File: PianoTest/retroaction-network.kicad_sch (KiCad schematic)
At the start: 64 parts, among them U201 MCP23S17-E/ML, U202 TMUX1112RSVR, U203 TMUX1112RSVR, U204 BGSA142GN12, U205 BGSA142GN12

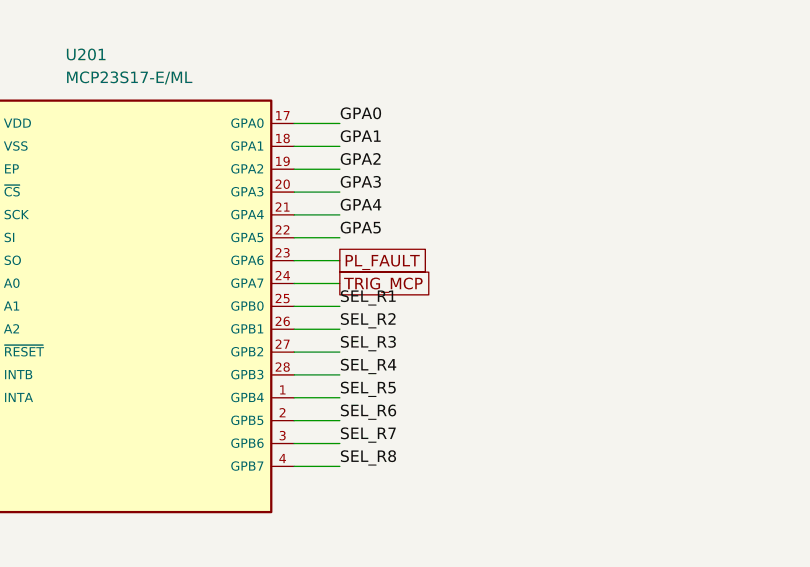
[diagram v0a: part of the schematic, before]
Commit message: PianoTest: discriminatore, latch e rilevatore di picco
Comparatore TLV3501 su SHAPER_OUT con soglia dal canale B del DAC61402
(partitore 22k/10k, BAT54S), latch 74LVC1G74 su GPA7 dell'MCP (ALERT#),
uscita HIT su TP e SMA. Rilevatore di picco OPA2365 + BAS416 + hold 1 nF
C0G prima dell'ADS8326, con reset da accesso SPI all'indirizzo 3 e
ponticello 0R per scavalcarlo. Trigger del LED dallo strobe dell'indirizzo 4.
Articolo: sezione 3.1 (formatore e acquisizione) aggiornata e ricompilata.
ERC 0.

Co-Authored-By: Claude Opus 5.5 (1M context) <noreply@anthropic.com>
Claude-Session: https://claude.ai/code/session_01J3krgWFTUEjwvCnwUp9cQn
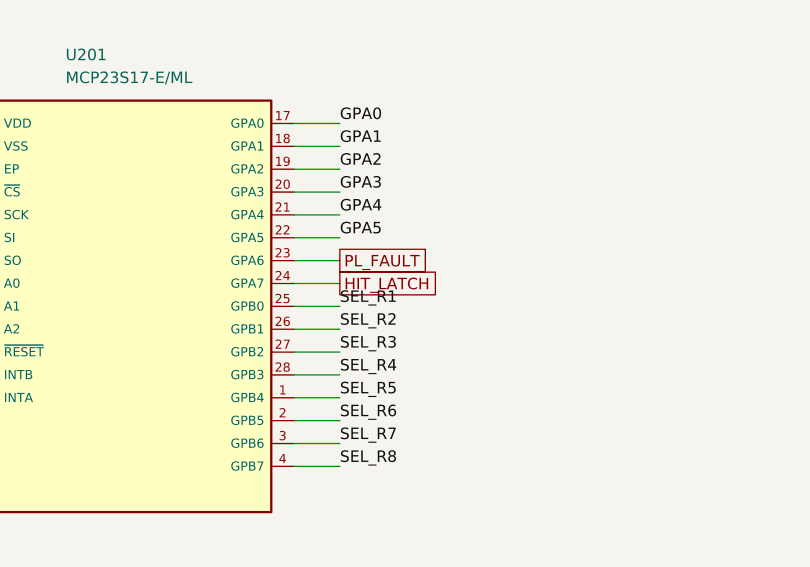
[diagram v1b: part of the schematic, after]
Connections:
- net TRIG_MCP renamed HIT_LATCH
